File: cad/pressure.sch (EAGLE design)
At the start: 10 parts, among them U1 WEMOS-D1-MINI, U2 ABPSENSOR, U3 BATTERY-CHARGER-LI-PROT

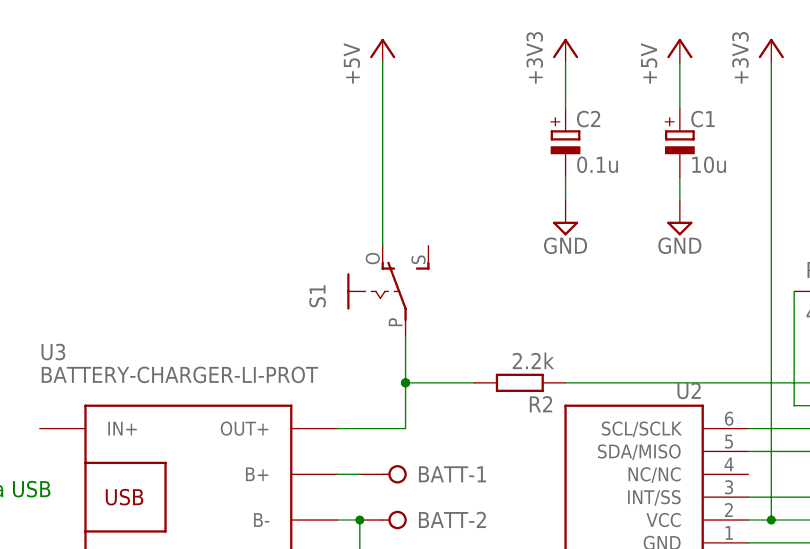
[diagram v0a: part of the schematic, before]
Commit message: Added pressure sensor settings to status
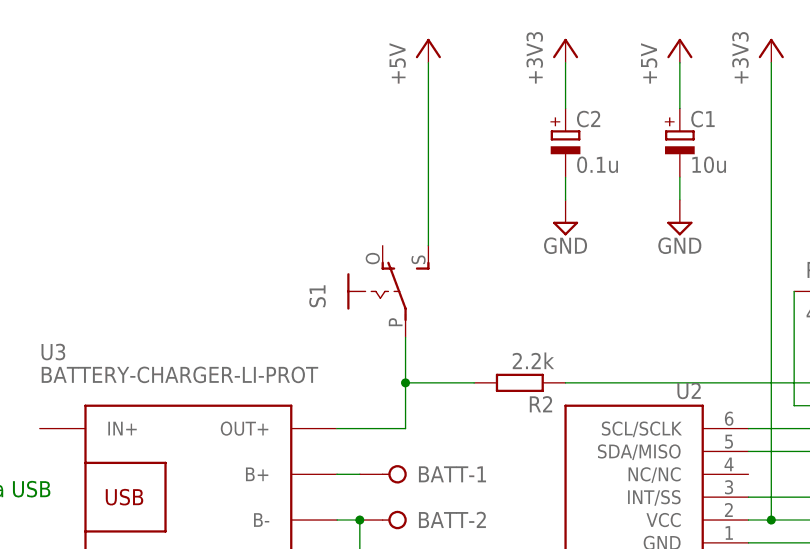
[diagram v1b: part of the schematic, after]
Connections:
- net +5V: now also S1.S; no longer S1.O
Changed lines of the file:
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@@
 <layer number="18" name="Vias" color="2" fill="1" visible="no" active="no"/>
 <layer number="19" name="Unrouted" color="6" fill="1" visible="no" active="no"/>
-<layer number="20" name="Dimension" color="15" fill="1" visible="no" active="no"/>
+<layer number="20" name="Dimension" color="24" fill="1" visible="no" active="no"/>
 <layer number="21" name="tPlace" color="7" fill="1" visible="no" active="no"/>
 <layer number="22" name="bPlace" color="7" fill="1" visible="no" active="no"/>
 <layer number="23" name="tOrigins" color="15" fill="1" visible="no" active="no"/>
 <layer number="24" name="bOrigins" color="15" fill="1" visible="no" active="no"/>
-<layer number="25" name="tNames" color="3" fill="1" visible="no" active="no"/>
+<layer number="25" name="tNames" color="7" fill="1" visible="no" active="no"/>
 <layer number="26" name="bNames" color="7" fill="1" visible="no" active="no"/>
-<layer number="27" name="tValues" color="15" fill="1" visible="no" active="no"/>
-<layer number="28" name="bValues" color="15" fill="1" visible="no" active="no"/>
+<layer number="27" name="tValues" color="7" fill="1" visible="no" active="no"/>
+<layer number="28" name="bValues" color="7" fill="1" visible="no" active="no"/>
 <layer number="29" name="tStop" color="7" fill="3" visible="no" active="no"/>
 <layer number="30" name="bStop" color="7" fill="6" visible="no" active="no"/>
@@
 <classes>
 <class number="0" name="default" width="0" drill="0">
+<clearance class="0" value="0.205"/>
 </class>
 </classes>
@@
 <attribute name="VALUE" x="-38.1" y="60.96" size="1.778" layer="96"/>
 </instance>
-<instance part="P+3" gate="1" x="0" y="99.06" smashed="yes">
-<attribute name="VALUE" x="-2.54" y="93.98" size="1.778" layer="96" rot="R90"/>
+<instance part="P+3" gate="1" x="5.08" y="99.06" smashed="yes">
+<attribute name="VALUE" x="2.54" y="93.98" size="1.778" layer="96" rot="R90"/>
 </instance>
 <instance part="SUPPLY6" gate="G$1" x="-38.1" y="33.02" smashed="yes">
@@
 </segment>
 <segment>
-<pinref part="S1" gate="1" pin="O"/>
+<pinref part="S1" gate="1" pin="S"/>
+<wire x1="5.08" y1="76.2" x2="5.08" y2="96.52" width="0.1524" layer="91"/>
 <pinref part="P+3" gate="1" pin="+5V"/>
-<wire x1="0" y1="76.2" x2="0" y2="96.52" width="0.1524" layer="91"/>
 </segment>
 </net>
@@
 <pinref part="R2" gate="G$1" pin="2"/>
 <wire x1="2.54" y1="60.96" x2="2.54" y2="66.04" width="0.1524" layer="91"/>
-<wire x1="2.54" y1="60.96" x2="10.16" y2="60.96" width="0.1524" layer="91"/>
+<wire x1="10.16" y1="60.96" x2="2.54" y2="60.96" width="0.1524" layer="91"/>
 <junction x="2.54" y="60.96"/>
 </segment>
@@
 </segment>
 </net>
-<net name="N$11" class="0">
-<segment>
-<junction x="2.54" y="60.96"/>
-</segment>
-</net>
